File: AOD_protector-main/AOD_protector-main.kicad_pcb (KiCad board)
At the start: 4 copper layers, 35 x 23 mm, 33 parts, among them IC1 MAX9141ESA+, J1 Input, J2 5V from source, J3 Output, J4 to fault handler, Q1 BSS316N, Q2 BSS316N, Q3 BSS316N, SW1 SW_Push, U1 REF35102QDBVR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

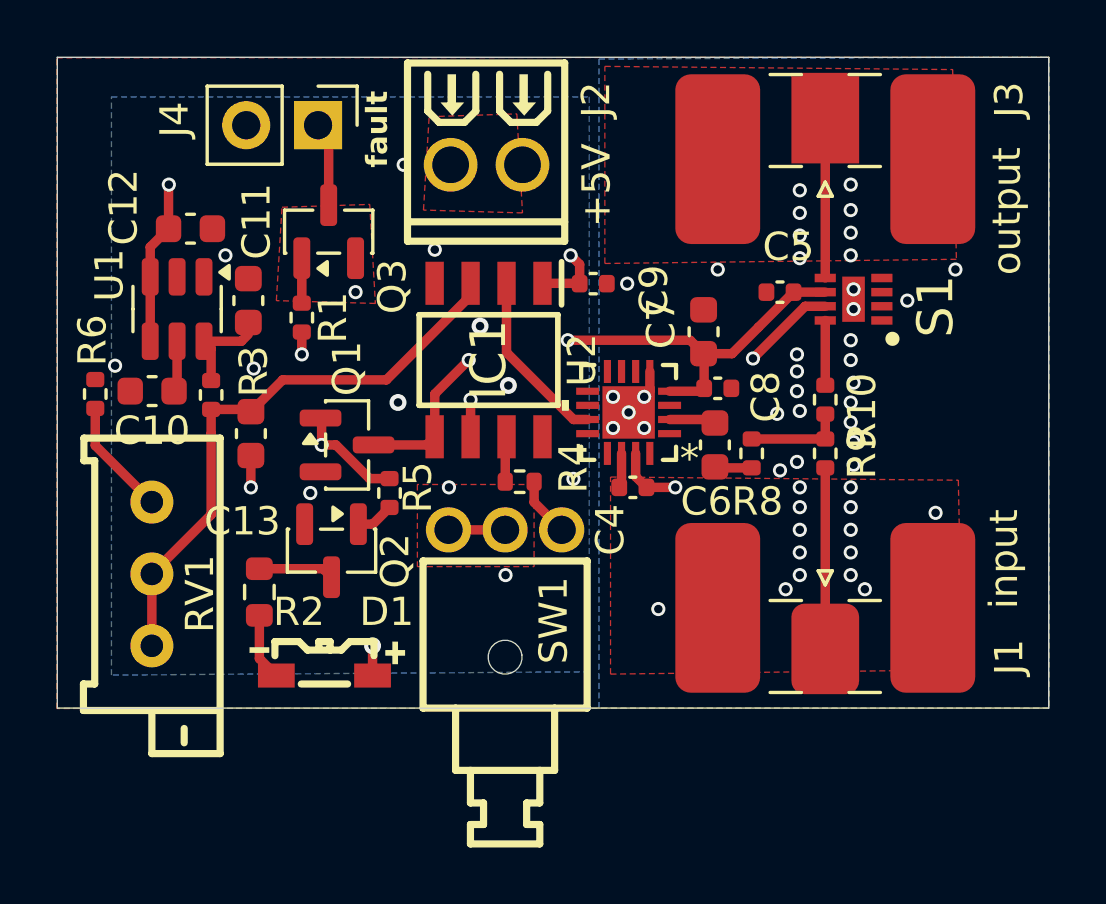
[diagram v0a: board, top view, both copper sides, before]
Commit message: Fixed a resistor value bug
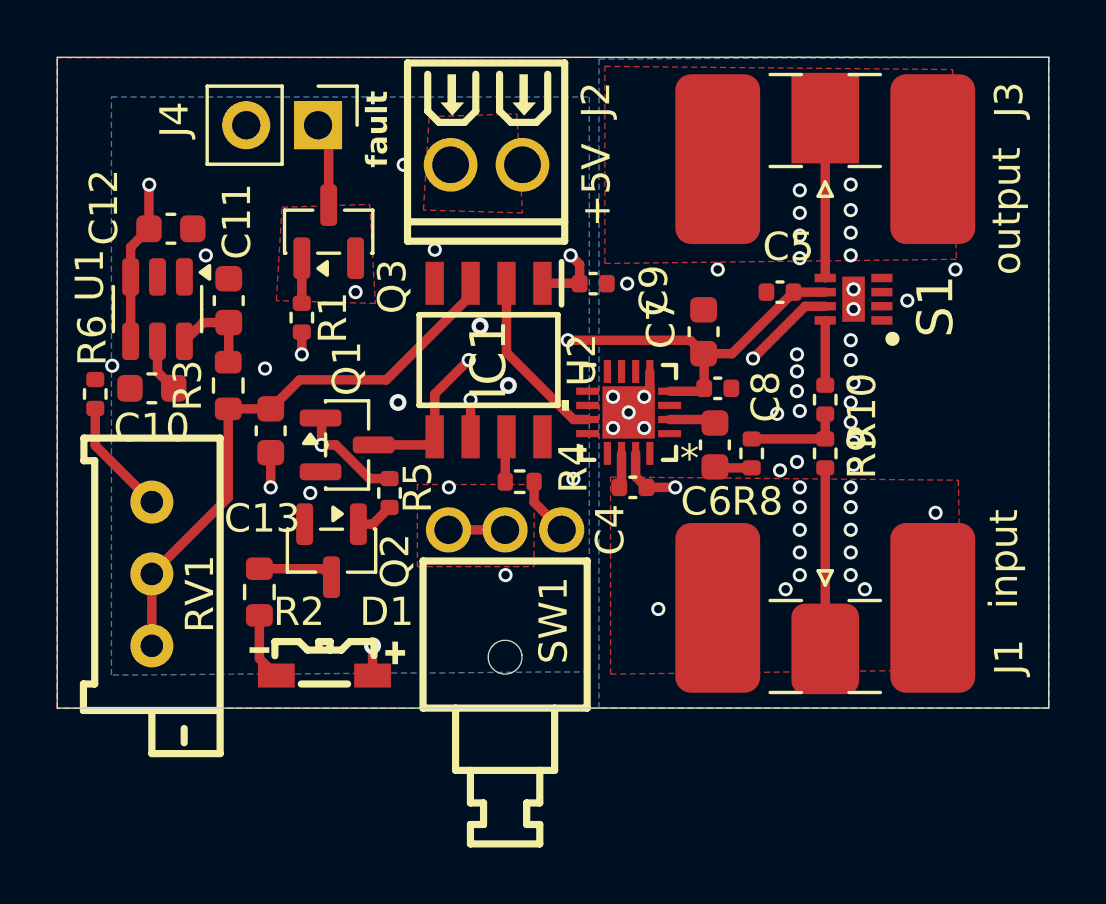
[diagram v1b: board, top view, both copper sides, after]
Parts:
- R3: value 51k -> 1.2M; footprint Resistor_SMD:R_0402_1005Metric -> Resistor_SMD:R_0603_1608Metric
- R6: value 15k -> 59k
- moved C13 0.71 mm to (105.8, 72.2)
- moved C11 0.69 mm to (104.3, 67.6)
- moved C12 0.69 mm to (102.3, 65.1)
- moved U1 0.69 mm to (101.8, 67.9)
- moved R3 0.69 mm to (104.3, 70.6)
- moved C10 0.10 mm to (101.6, 70.7)
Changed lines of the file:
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@@
 		)
 	)
-	(footprint "Resistor_SMD:R_0402_1005Metric"
+	(footprint "Resistor_SMD:R_0603_1608Metric"
 		(layer "F.Cu")
-		(at 103.694967 70.934967 90)
-		(descr "Resistor SMD 0402 (1005 Metric), square (rectangular) end terminal, IPC-7351 nominal, (Body size source: IPC-SM-782 page 72, https://www.pcb-3d.com/wordpress/wp-content/uploads/ipc-sm-782a_amendment_1_and_2.pdf), generated with kicad-footprint-generator")
+		(at 104.3 70.6 90)
+		(descr "Resistor SMD 0603 (1608 Metric), square (rectangular) end terminal, IPC-7351 nominal, (Body size source: IPC-SM-782 page 72, https://www.pcb-3d.com/wordpress/wp-content/uploads/ipc-sm-782a_amendment_1_and_2.pdf), generated with kicad-footprint-generator")
 		(tags "resistor")
 		(property "Reference" "R3"
-			(at 0.834967 1.505033 90)
+			(at 0 -1.43 90)
 			(layer "F.SilkS")
 			(effects
@@
 			)
 		)
-		(property "Value" "51k"
-			(at 0 1.17 90)
+		(property "Value" "1.2M"
+			(at 0 1.43 90)
 			(layer "F.Fab")
 			(effects
@@
 			)
 		)
-		(property "Part number" "RT0402BRD0751KL"
+		(property "Part number" " MCT0603MD1204BP500"
 			(at 0 0 90)
 			(unlocked yes)
@@
 			)
 		)
-		(property "JLCPCB Part" "C852828"
+		(property "JLCPCB Part" "C3933664"
 			(at 0 0 90)
 			(unlocked yes)
@@
 		(attr smd)
 		(fp_line
-			(start -0.153641 -0.38)
-			(end 0.153641 -0.38)
+			(start -0.237258 -0.5225)
+			(end 0.237258 -0.5225)
 			(stroke
 				(width 0.12)
@@
 		)
 		(fp_line
-			(start -0.153641 0.38)
-			(end 0.153641 0.38)
+			(start -0.237258 0.5225)
+			(end 0.237258 0.5225)
 			(stroke
 				(width 0.12)
@@
 		)
 		(fp_line
-			(start 0.93 -0.47)
-			(end 0.93 0.47)
+			(start 1.48 -0.73)
+			(end 1.48 0.73)
 			(stroke
 				(width 0.05)
@@
 		)
 		(fp_line
-			(start -0.93 -0.47)
-			(end 0.93 -0.47)
+			(start -1.48 -0.73)
+			(end 1.48 -0.73)
 			(stroke
 				(width 0.05)
@@
 		)
 		(fp_line
-			(start 0.93 0.47)
-			(end -0.93 0.47)
+			(start 1.48 0.73)
+			(end -1.48 0.73)
 			(stroke
 				(width 0.05)
@@
 		)
 		(fp_line
-			(start -0.93 0.47)
-			(end -0.93 -0.47)
+			(start -1.48 0.73)
+			(end -1.48 -0.73)
 			(stroke
 				(width 0.05)
@@
 		)
 		(fp_line
-			(start 0.525 -0.27)
-			(end 0.525 0.27)
+			(start 0.8 -0.4125)
+			(end 0.8 0.4125)
 			(stroke
 				(width 0.1)
@@
 		)
 		(fp_line
-			(start -0.525 -0.27)
-			(end 0.525 -0.27)
+			(start -0.8 -0.4125)
+			(end 0.8 -0.4125)
 			(stroke
 				(width 0.1)
@@
 		)
 		(fp_line
-			(start 0.525 0.27)
-			(end -0.525 0.27)
+			(start 0.8 0.4125)
+			(end -0.8 0.4125)
 			(stroke
 				(width 0.1)
@@
 		)
 		(fp_line
-			(start -0.525 0.27)
-			(end -0.525 -0.27)
+			(start -0.8 0.4125)
+			(end -0.8 -0.4125)
 			(stroke
 				(width 0.1)
@@
 			(effects
 				(font
-					(size 0.26 0.26)
-					(thickness 0.04)
+					(size 0.4 0.4)
+					(thickness 0.06)
 				)
 			)
 		)
 		(pad "1" smd roundrect
-			(at -0.51 0 90)
-			(size 0.54 0.64)
+			(at -0.825 0 90)
+			(size 0.8 0.95)
 			(layers "F.Cu" "F.Mask" "F.Paste")
 			(roundrect_rratio 0.25)
@@
 		)
 		(pad "2" smd roundrect
-			(at 0.51 0 90)
-			(size 0.54 0.64)
+			(at 0.825 0 90)
+			(size 0.8 0.95)
 			(layers "F.Cu" "F.Mask" "F.Paste")
 			(roundrect_rratio 0.25)
@@
 		)
 		(embedded_fonts no)
-		(model "${KICAD9_3DMODEL_DIR}/Resistor_SMD.3dshapes/R_0402_1005Metric.step"
+		(model "${KICAD9_3DMODEL_DIR}/Resistor_SMD.3dshapes/R_0603_1608Metric.step"
 			(offset
 				(xyz 0 0 0)
@@
 			)
 		)
-		(property "Value" "15k"
+		(property "Value" "59k"
 			(at 0 1.17 90)
 			(layer "F.Fab")
@@
 			)
 		)
-		(property "Part number" "TC02G1502BT"
+		(property "Part number" "RT0402BRD0759KL"
 			(at 0 0 270)
 			(unlocked yes)
@@
 			)
 		)
-		(property "JLCPCB Part" "C20627044"
+		(property "JLCPCB Part" "C852853"
 			(at 0 0 270)
 			(unlocked yes)
@@
 	(footprint "Capacitor_SMD:C_0603_1608Metric"
 		(layer "F.Cu")
-		(at 102.964967 65.057967 180)
+		(at 102.273 65.0605 180)
 		(descr "Capacitor SMD 0603 (1608 Metric), square (rectangular) end terminal, IPC_7351 nominal, (Body size source: IPC-SM-782 page 76, https://www.pcb-3d.com/wordpress/wp-content/uploads/ipc-sm-782a_amendment_1_and_2.pdf), generated with kicad-footprint-generator")
 		(tags "capacitor")
@@
 	(footprint "Capacitor_SMD:C_0603_1608Metric"
 		(layer "F.Cu")
-		(at 101.609967 70.797967 180)
+		(at 101.6 70.7 180)
 		(descr "Capacitor SMD 0603 (1608 Metric), square (rectangular) end terminal, IPC_7351 nominal, (Body size source: IPC-SM-782 page 76, https://www.pcb-3d.com/wordpress/wp-content/uploads/ipc-sm-782a_amendment_1_and_2.pdf), generated with kicad-footprint-generator")
 		(tags "capacitor")
@@
 	(footprint "Capacitor_SMD:C_0603_1608Metric"
 		(layer "F.Cu")
-		(at 105.1 72.3 90)
+		(at 105.8 72.2 90)
 		(descr "Capacitor SMD 0603 (1608 Metric), square (rectangular) end terminal, IPC_7351 nominal, (Body size source: IPC-SM-782 page 76, https://www.pcb-3d.com/wordpress/wp-content/uploads/ipc-sm-782a_amendment_1_and_2.pdf), generated with kicad-footprint-generator")
 		(tags "capacitor")
@@
 	(footprint "Package_TO_SOT_SMD:SOT-23-6"
 		(layer "F.Cu")
-		(at 102.491967 67.897467 -90)
+		(at 101.8 67.9 -90)
 		(descr "SOT, 6 Pin (JEDEC MO-178 Var AB https://www.jedec.org/document_search?search_api_views_fulltext=MO-178), generated with kicad-footprint-generator ipc_gullwing_generator.py")
 		(tags "SOT TO_SOT_SMD")
@@
 	(footprint "Capacitor_SMD:C_0603_1608Metric"
 		(layer "F.Cu")
-		(at 105.009967 67.597967 -90)
+		(at 104.318 67.6005 -90)
 		(descr "Capacitor SMD 0603 (1608 Metric), square (rectangular) end terminal, IPC_7351 nominal, (Body size source: IPC-SM-782 page 76, https://www.pcb-3d.com/wordpress/wp-content/uploads/ipc-sm-782a_amendment_1_and_2.pdf), generated with kicad-footprint-generator")
 		(tags "capacitor")
@@
 	)
 	(segment
-		(start 101.541967 69.034967)
-		(end 101.541967 66.759967)
-		(width 0.3348)
-		(layer "F.Cu")
-		(net 1)
-	)
-	(segment
-		(start 105.1 73.075)
-		(end 105.1 74.2)
+		(start 100.85 69.0375)
+		(end 100.85 66.7625)
 		(width 0.3348)
 		(layer "F.Cu")
@@
 	)
 	(segment
-		(start 102.189967 65.057967)
-		(end 102.189967 63.510033)
+		(start 101.498 65.0605)
+		(end 101.498 63.512566)
 		(width 0.3348)
 		(layer "F.Cu")
@@
 	)
 	(segment
-		(start 101.541967 65.705967)
-		(end 101.541967 66.759967)
+		(start 100.85 65.7085)
+		(end 100.85 66.7625)
 		(width 0.3348)
 		(layer "F.Cu")
@@
 	)
 	(segment
+		(start 105.8 74.2)
+		(end 105.8 72.975)
+		(width 0.3348)
+		(layer "F.Cu")
+		(net 1)
+	)
+	(segment
 		(start 120.625 69)
 		(end 121.1 69.475)
@@
 	)
 	(segment
-		(start 102.189967 63.510033)
-		(end 102.2 63.5)
+		(start 101.498 63.512566)
+		(end 101.508033 63.502533)
 		(width 0.3348)
 		(layer "F.Cu")
@@
 	)
 	(segment
-		(start 102.189967 65.057967)
-		(end 101.541967 65.705967)
+		(start 101.498 65.0605)
+		(end 100.85 65.7085)
 		(width 0.3348)
 		(layer "F.Cu")
@@
 	)
 	(via
-		(at 102.2 63.5)
+		(at 101.508033 63.502533)
 		(size 0.5)
 		(drill 0.3)
@@
 	)
 	(via
-		(at 105.1 74.2)
+		(at 105.8 74.2)
 		(size 0.5)
 		(drill 0.3)
@@
 	)
 	(via
-		(at 105.2 70)
+		(at 105.6 70)
 		(size 0.5)
 		(drill 0.3)
@@
 	)
 	(via
-		(at 104.2 66)
+		(at 103.508033 66.002533)
 		(size 0.5)
 		(drill 0.3)
@@
 	)
 	(via
-		(at 100.3 69.9)
+		(at 100.2 69.9)
 		(size 0.5)
 		(drill 0.3)
@@
 	)
 	(segment
-		(start 102.491967 69.034967)
-		(end 102.491967 70.690967)
+		(start 101.8 70.125)
+		(end 102.375 70.7)
 		(width 0.3348)
 		(layer "F.Cu")
@@
 	)
 	(segment
-		(start 102.491967 70.690967)
-		(end 102.384967 70.797967)
+		(start 101.8 69.0375)
+		(end 101.8 70.125)
 		(width 0.3348)
 		(layer "F.Cu")
@@
 	)
 	(segment
-		(start 103.694967 70.424967)
-		(end 103.694967 69.287967)
+		(start 104.318 68.3755)
+		(end 103.412 68.3755)
 		(width 0.3348)
 		(layer "F.Cu")
@@
 	)
 	(segment
-		(start 104.765033 69.034967)
-		(end 103.441967 69.034967)
+		(start 103.412 68.3755)
+		(end 102.75 69.0375)
 		(width 0.3348)
 		(layer "F.Cu")
@@
 	)
 	(segment
-		(start 105.009967 68.790033)
-		(end 104.765033 69.034967)
+		(start 104.318 68.3755)
+		(end 104.318 69.757)
 		(width 0.3348)
 		(layer "F.Cu")
@@
 	)
 	(segment
-		(start 103.694967 69.287967)
-		(end 103.441967 69.034967)
+		(start 104.318 69.757)
+		(end 104.3 69.775)
 		(width 0.3348)
 		(layer "F.Cu")
@@
 	)
 	(segment
-		(start 103.694967 72.3)
-		(end 103.694967 75.165033)
-		(width 0.3348)
-		(layer "F.Cu")
-		(net 8)
-	)
-	(segment
-		(start 106.225 70.4)
-		(end 105.1 71.525)
-		(width 0.3348)
-		(layer "F.Cu")
-		(net 8)
-	)
-	(segment
 		(start 112.865 67.4255)
 		(end 109.8905 70.4)
@@
 	)
 	(segment
-		(start 103.694967 71.444967)
-		(end 103.694967 72.3)
+		(start 101.6 77.26)
+		(end 104.3 74.56)
 		(width 0.3348)
 		(layer "F.Cu")
@@
 	)
 	(segment
-		(start 105.019967 71.444967)
-		(end 105.1 71.525)
+		(start 104.3 74.56)
+		(end 104.3 71.425)
 		(width 0.3348)
 		(layer "F.Cu")
@@
 	)
 	(segment
-		(start 103.694967 75.165033)
-		(end 101.6 77.26)
+		(start 105.8 71.425)
+		(end 106.825 70.4)
 		(width 0.3348)
 		(layer "F.Cu")
@@
 	)
 	(segment
-		(start 109.8905 70.4)
-		(end 106.225 70.4)
+		(start 106.825 70.4)
+		(end 109.8905 70.4)
 		(width 0.3348)
 		(layer "F.Cu")
@@
 	)
 	(segment
-		(start 103.694967 71.444967)
-		(end 105.019967 71.444967)
+		(start 105.8 71.425)
+		(end 104.3 71.425)
 		(width 0.3348)
 		(layer "F.Cu")
